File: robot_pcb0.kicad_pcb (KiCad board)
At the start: 2 copper layers, 74 parts, among them J1 USB_B_Mini, J10 GPIO, J2 CAN, J3 PWR, J4 Power_terminal, J5 Motor1, J6 Motor2, J7 Motor3, J8 Motor4, J9 UART, P1 SWD, U1 TJA1051TK-3, U2 STM32F40X_LQFP64, U3 MPU9250, U4 MCP16311/2, U5 MCP16311/2, U6 DRV8833PW, U7 DRV8833PW, Y1 8M

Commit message: some routing
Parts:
- moved C19 1.08 mm to (131.6, 95.2)
- moved C17 0.89 mm to (135.1, 95.2)
- turned C30 to 0 degrees
- turned C32 to 0 degrees
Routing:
- net Net-(C21-Pad2): track 0.00 -> 8.27 mm
- net Net-(R6-Pad1): track 0.00 -> 6.70 mm
- net Net-(C22-Pad2): track 0.00 -> 5.19 mm
- net 5V: track 0.00 -> 4.37 mm
- net Net-(C21-Pad1): track 0.00 -> 3.08 mm
- net Net-(C19-Pad1): track 0.00 -> 2.76 mm
- net V_IN: track 0.00 -> 0.77 mm
- net Net-(R7-Pad1): track 0.00 -> 0.57 mm
- added copper zone on B.Cu, net GND
- added copper zone on F.Cu, net VCC
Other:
- board outline added: 63.5 x 59.7 mm

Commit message: small amount of routing
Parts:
- moved C19 6.15 mm to (130.5, 89.2), turned to 90 degrees
- moved C17 4.56 mm to (136.2, 90.8), turned to 90 degrees
- moved R6 2.45 mm to (127.9, 88.5)
- moved R8 2.17 mm to (127.9, 91.3), turned to 180 degrees
- moved C29 1.49 mm to (99.6, 109.3)
- moved C31 1.32 mm to (96.5, 109.3), turned to 180 degrees
- moved C28 0.94 mm to (101.9, 111.8)
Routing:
- net VCC: track 0.05 -> 41.6 mm
- net GND: track 15.3 -> 43.0 mm
- net Net-(J8-Pad2): track 0.00 -> 18.8 mm
- net Net-(J8-Pad1): track 0.00 -> 12.6 mm
- net 5V: track 4.37 -> 13.7 mm
- net Net-(J7-Pad2): track 0.00 -> 9.28 mm
- net Net-(J7-Pad1): track 0.00 -> 7.75 mm
- net V_IN: track 0.77 -> 6.92 mm
- net Net-(C28-Pad2): track 0.00 -> 4.22 mm
- net Net-(R6-Pad1): track 6.70 -> 9.20 mm
- net Net-(C19-Pad1): track 2.76 -> 4.32 mm
- removed copper zone on B.Cu, net GND
- removed copper zone on F.Cu, net VCC

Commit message: update
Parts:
- removed C14: 100n, Capacitor_SMD:C_0603_1608Metric
- R11: value 51k -> 56k
- U3: value MPU9250 -> BMI160; footprint crf1:QFN-24-1EP_3x3mm_P0.4mm_nopp -> Package_LGA:Bosch_LGA-14_3x2.5mm_P0.5mm
- moved R10 37.3 mm to (99.3, 119.4), turned to 0 degrees
- moved R3 7.73 mm to (100.1, 78.7), turned to 180 degrees
- moved C19 6.15 mm to (131.6, 95.2), turned to 180 degrees
- moved C13 4.49 mm to (108.6, 107.7), turned to 0 degrees
- moved C6 4.39 mm to (111.1, 107.2), turned to 270 degrees
- moved U3 2.87 mm to (108.4, 105.2)
- moved C11 2.76 mm to (112.3, 99.1), turned to 180 degrees
- moved R8 2.69 mm to (129.8, 93.2), turned to 0 degrees
- moved R5 2.52 mm to (106.0, 101.3), turned to 180 degrees
- moved R6 2.45 mm to (128.2, 90.9)
- moved C16 2.00 mm to (112.2, 84.1), turned to 0 degrees
- moved R4 1.65 mm to (109.3, 101.3), turned to 0 degrees
- moved C29 1.49 mm to (100.3, 108.0)
- moved C31 1.32 mm to (96.5, 108.0), turned to 0 degrees
- moved C28 0.94 mm to (102.9, 111.8)
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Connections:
- U2 pad 57: Net-(U2-Pad57) -> IMU_INT2
- U3 pad 1: VCC -> GND
- U3 pad 11: GND -> Net-(U3-Pad11)
- U3 pad 12: Net-(U3-Pad12) -> VCC
- U3 pad 13: VCC -> SCL
- U3 pad 14: (no net) -> SDA
- U3 pad 2: (no net) -> Net-(U3-Pad2)
- U3 pad 3: (no net) -> Net-(U3-Pad3)
- U3 pad 4: (no net) -> Net-(U3-Pad4)
- U3 pad 5: (no net) -> VCC
- U3 pad 6: (no net) -> GND
- U3 pad 7: Net-(U3-Pad7) -> GND
- U3 pad 9: GND -> IMU_INT2
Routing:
- net VCC: track 41.6 -> 7.31 mm
- net CANL: track 0.00 -> 27.6 mm, vias 0 -> 2
- net CANH: track 0.00 -> 26.2 mm, vias 0 -> 2
- net GPIO0: track 0.00 -> 20.7 mm
- net GPIO1: track 0.00 -> 20.1 mm
- net GPIO6: track 0.00 -> 18.9 mm, vias 0 -> 1
- net Net-(J8-Pad2): track 18.8 -> 0.00 mm
- net GPIO7: track 0.00 -> 18.0 mm, vias 0 -> 1
- net GPIO2: track 0.00 -> 17.3 mm
- net GPIO4: track 0.00 -> 16.6 mm
- net GPIO3: track 0.00 -> 16.6 mm
- net GPIO5: track 0.00 -> 16.0 mm
- net 5V: track 13.7 -> 0.00 mm
- net Net-(J8-Pad1): track 12.6 -> 0.00 mm
- net GND: track 43.0 -> 30.5 mm, vias 2 -> 0
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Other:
- board outline removed

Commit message: routing
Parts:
- moved C30 21.7 mm to (99.7, 108.6), turned to 90 degrees
- moved C29 21.0 mm to (121.3, 108.4), turned to 90 degrees
- moved R10 15.7 mm to (101.9, 103.9)
- moved C15 10.0 mm to (94.3, 91.5), turned to 180 degrees
- moved C9 8.40 mm to (117.3, 88.1)
- moved U1 5.69 mm to (94.2, 94.7), turned to 90 degrees
- moved C18 5.55 mm to (135.6, 111.8), turned to 90 degrees
- moved C20 5.11 mm to (130.3, 112.0), turned to 90 degrees
- moved C19 4.44 mm to (130.6, 90.9), turned to 90 degrees
- moved R11 4.17 mm to (121.9, 103.6), turned to 270 degrees
- moved C2 3.85 mm to (94.3, 97.8), turned to 180 degrees
- moved C27 3.62 mm to (123.1, 108.4)
- moved C28 3.49 mm to (101.4, 108.6)
- moved R8 2.51 mm to (128.0, 91.4)
- moved R12 1.70 mm to (119.1, 103.6), turned to 270 degrees
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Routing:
- net GND: track 30.5 -> 297.3 mm, vias 0 -> 4
- net VCC: track 7.31 -> 169.7 mm, vias 0 -> 5
- net 5V: track 0.00 -> 111.4 mm, vias 0 -> 5
- net V_IN: track 0.00 -> 88.4 mm, vias 0 -> 3
- net DRV_nFAULT: track 0.00 -> 64.1 mm, vias 0 -> 4
- net DRV_BIN2_1: track 0.00 -> 35.4 mm, vias 0 -> 4
- net NRST: track 0.00 -> 34.2 mm, vias 0 -> 2
- net DRV_BIN1_1: track 0.00 -> 31.7 mm, vias 0 -> 4
- net DRV_AIN1_2: track 0.00 -> 28.7 mm, vias 0 -> 2
- net UART_RXD: track 0.00 -> 28.3 mm, vias 0 -> 1
- net UART_TXD: track 0.00 -> 28.2 mm, vias 0 -> 1
- net DRV_AIN2_1: track 0.00 -> 28.0 mm, vias 0 -> 2
- net DRV_AIN1_1: track 0.00 -> 27.8 mm, vias 0 -> 2
- net DRV_AIN2_2: track 0.00 -> 26.3 mm, vias 0 -> 2
- net DRV_BIN1_2: track 0.00 -> 25.7 mm, vias 0 -> 2
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
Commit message: routed and filled
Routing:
- net VCC: track 169.7 -> 277.3 mm, vias 5 -> 11
- net GND: track 297.3 -> 373.7 mm, vias 4 -> 21
- net 5V: track 111.4 -> 129.6 mm, vias 5 -> 3
- net IMU_INT2: track 16.4 -> 15.3 mm
- net SWCLK: track 17.1 -> 18.0 mm
- net UART_TXD: track 28.2 -> 29.0 mm
- net UART_RXD: track 28.3 -> 29.0 mm
- net SWDIO: track 21.3 -> 21.9 mm
- added copper zone on B.Cu, net GND
- added copper zone on F.Cu, net GND
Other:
- board outline added: 61.9 x 57.8 mm

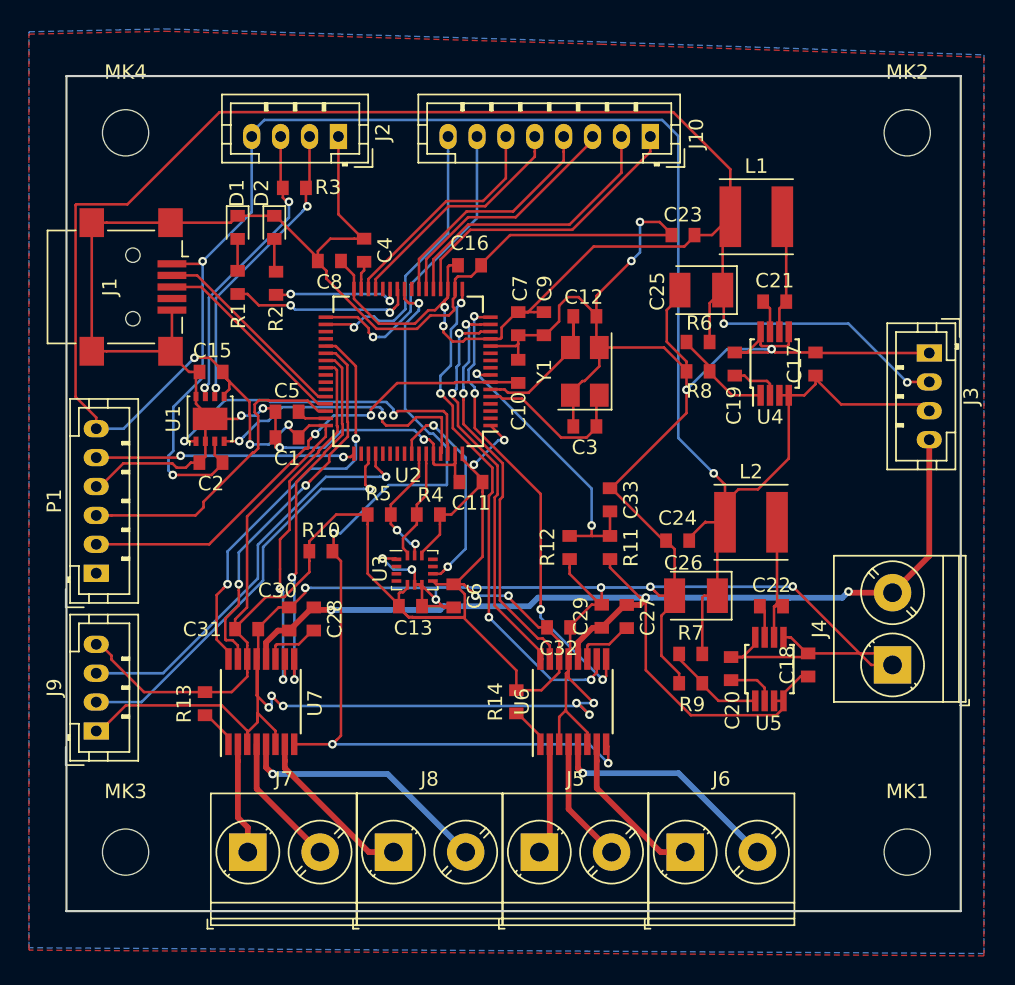
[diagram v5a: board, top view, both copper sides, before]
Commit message: added some extra vias and shortened a 5V path
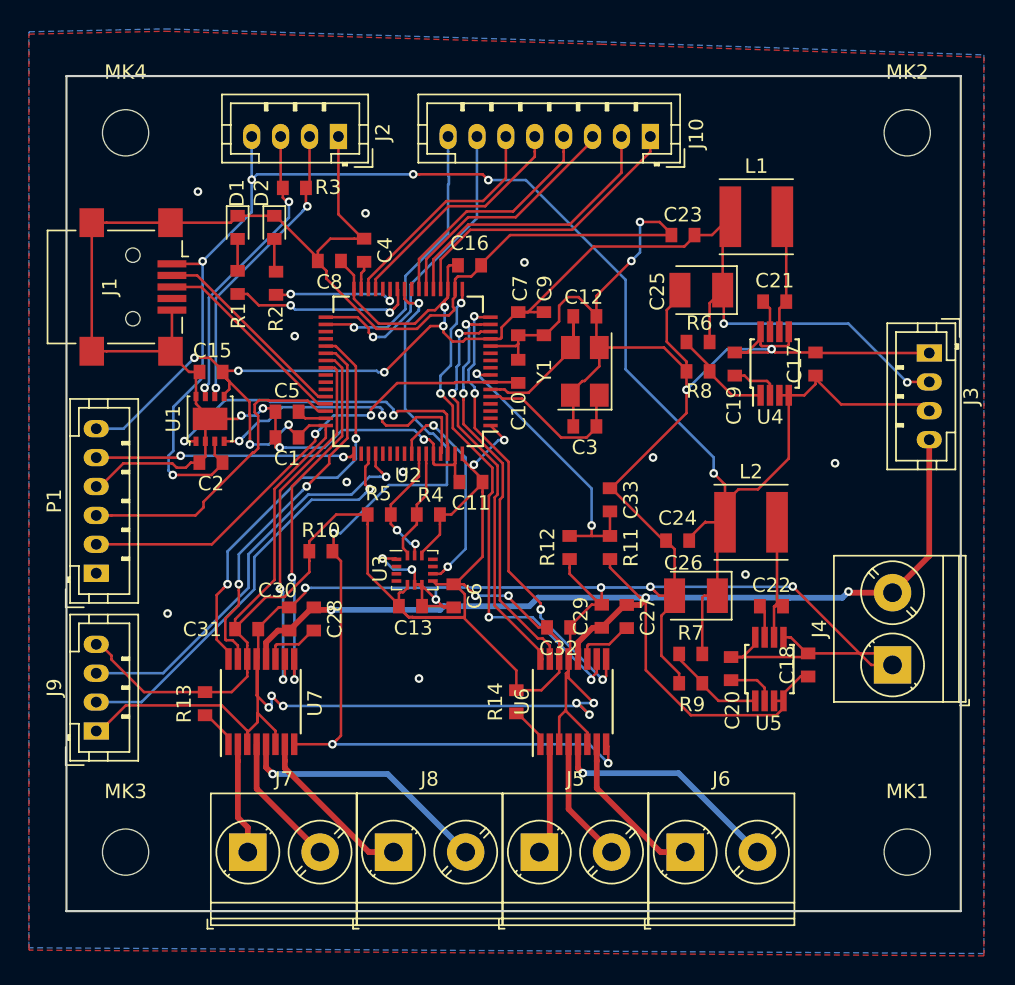
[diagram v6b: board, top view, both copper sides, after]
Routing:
- net VCC: track 277.3 -> 225.0 mm, vias 11 -> 13
- net 5V: track 129.6 -> 119.6 mm, vias 3 -> 6
- net GND: vias 21 -> 32

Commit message: rounded corners and some more vias between groundplanes
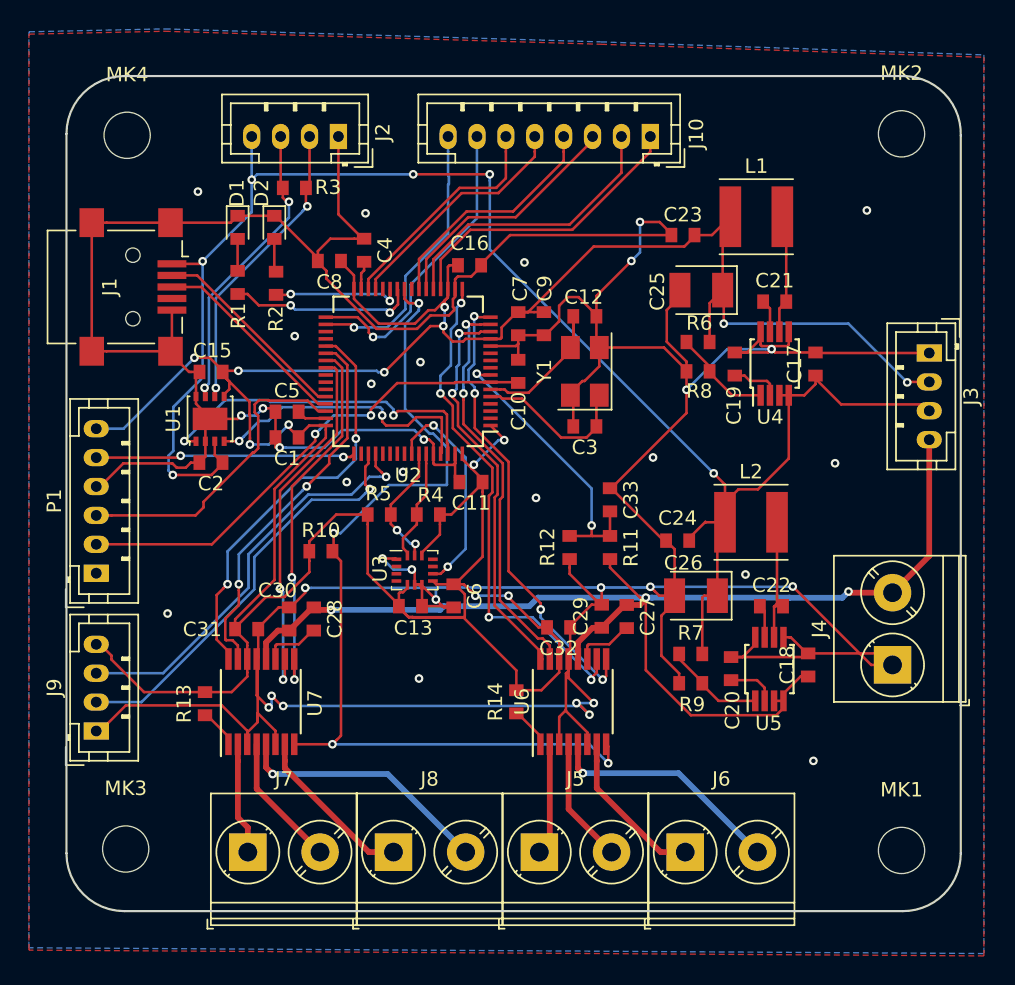
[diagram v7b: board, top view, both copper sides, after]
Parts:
- moved MK1 0.41 mm to (142.1, 124.6)
- moved MK2 0.40 mm to (142.1, 75.0)
- moved MK3 0.21 mm to (88.4, 124.5)
- moved MK4 0.20 mm to (88.5, 75.1)
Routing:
- net 5V: track 119.6 -> 118.4 mm
- net GND: vias 32 -> 37
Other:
- outline, holes or cut-outs redrawn
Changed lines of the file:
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@@
   (general
     (thickness 1.6)
-    (drawings 4)
-    (tracks 1098)
+    (drawings 8)
+    (tracks 1100)
     (modules 73)
     (nets 90)
@@
   )
   (module "MountingHole:MountingHole_3.2mm_M3" (layer "F.Cu")
-    (at 142.494 124.714)
+    (at 142.1 124.6)
     (descr "Mounting Hole 3.2mm, no annular, M3")
     (tags "mounting hole 3.2mm no annular m3")
@@
   )
   (module "MountingHole:MountingHole_3.2mm_M3" (layer "F.Cu")
-    (at 142.494 74.93)
+    (at 142.1 75)
     (descr "Mounting Hole 3.2mm, no annular, M3")
     (tags "mounting hole 3.2mm no annular m3")
@@
   )
   (module "MountingHole:MountingHole_3.2mm_M3" (layer "F.Cu")
-    (at 88.392 124.714)
+    (at 88.4 124.5)
     (descr "Mounting Hole 3.2mm, no annular, M3")
     (tags "mounting hole 3.2mm no annular m3")
@@
   )
   (module "MountingHole:MountingHole_3.2mm_M3" (layer "F.Cu")
-    (at 88.392 74.93)
+    (at 88.5 75.1)
     (descr "Mounting Hole 3.2mm, no annular, M3")
     (tags "mounting hole 3.2mm no annular m3")
@@
     )
   )
-  (gr_line (start 84.3 71) (end 146.2 71) (layer "Edge.Cuts") (width 0.15))
-  (gr_line (start 84.3 128.8) (end 84.3 71) (layer "Edge.Cuts") (width 0.15))
-  (gr_line (start 146.2 128.8) (end 84.3 128.8) (layer "Edge.Cuts") (width 0.15))
-  (gr_line (start 146.2 71) (end 146.2 128.8) (layer "Edge.Cuts") (width 0.15))
+  (gr_line (start 146.2 124.8) (end 146.199999 75.099999) (layer "Edge.Cuts") (width 0.15))
+  (gr_line (start 88.3 128.8) (end 142.2 128.8) (layer "Edge.Cuts") (width 0.15))
+  (gr_line (start 84.3 75) (end 84.3 124.8) (layer "Edge.Cuts") (width 0.15))
+  (gr_line (start 142.199999 70.998751) (end 88.3 71) (layer "Edge.Cuts") (width 0.15))
+  (gr_arc (start 142.2 124.8) (end 142.2 128.8) (angle -90) (layer "Edge.Cuts") (width 0.15))
+  (gr_arc (start 88.3 124.8) (end 84.3 124.8) (angle -90) (layer "Edge.Cuts") (width 0.15))
+  (gr_arc (start 88.3 75) (end 88.3 71) (angle -90) (layer "Edge.Cuts") (width 0.15))
+  (gr_arc (start 142.2 75) (end 146.199999 75.099999) (angle -91.43209618) (layer "Edge.Cuts") (width 0.15))
   (segment (start 117.755 123.9895) (end 117.0305 124.714) (width 0.4) (layer "F.Cu") (net 1))
   (segment (start 117.755 117.25) (end 117.755 123.9895) (width 0.4) (layer "F.Cu") (net 1))
@@
   (via (at 137.5 97.8) (size 0.6) (drill 0.3) (layers "F.Cu" "B.Cu") (net 8))
   (via (at 131.3 105.5) (size 0.6) (drill 0.3) (layers "F.Cu" "B.Cu") (net 8))
+  (via (at 136 118.4) (size 0.6) (drill 0.3) (layers "F.Cu" "B.Cu") (net 8))
+  (via (at 139.7 80.3) (size 0.6) (drill 0.3) (layers "F.Cu" "B.Cu") (net 8))
+  (via (at 108.8 90.8) (size 0.6) (drill 0.3) (layers "F.Cu" "B.Cu") (net 8))
+  (via (at 105.4 92.3) (size 0.6) (drill 0.3) (layers "F.Cu" "B.Cu") (net 8))
+  (via (at 116.8 100.2) (size 0.6) (drill 0.3) (layers "F.Cu" "B.Cu") (net 8))
   (segment (start 121.005 118.4) (end 121.005 117.25) (width 0.4) (layer "F.Cu") (net 9))
   (segment (start 121.005 120.292) (end 121.005 118.4) (width 0.4) (layer "F.Cu") (net 9))
@@
   (segment (start 129.881396 99.281396) (end 129.1 98.5) (width 0.18) (layer "F.Cu") (net 22))
   (segment (start 129.881396 101.885756) (end 129.881396 99.281396) (width 0.18) (layer "F.Cu") (net 22))
-  (segment (start 129.1 98.5) (end 129.1 97.4) (width 0.18) (layer "B.Cu") (net 22))
-  (segment (start 129.1 97.4) (end 123 91.3) (width 0.18) (layer "B.Cu") (net 22))
-  (segment (start 123 91.3) (end 123 85.1) (width 0.18) (layer "B.Cu") (net 22))
-  (via (at 113.5 78.2) (size 0.6) (drill 0.3) (layers "F.Cu" "B.Cu") (net 22))
-  (segment (start 123 85.1) (end 116.1 78.2) (width 0.18) (layer "B.Cu") (net 22))
-  (segment (start 116.1 78.2) (end 113.5 78.2) (width 0.18) (layer "B.Cu") (net 22))
-  (segment (start 113.5 78.2) (end 113.1 77.8) (width 0.18) (layer "F.Cu") (net 22))
   (via (at 108.3 77.8) (size 0.6) (drill 0.3) (layers "F.Cu" "B.Cu") (net 22))
-  (segment (start 108.724264 77.8) (end 108.3 77.8) (width 0.18) (layer "F.Cu") (net 22))
-  (segment (start 113.1 77.8) (end 108.724264 77.8) (width 0.18) (layer "F.Cu") (net 22))
   (segment (start 97.124 80.422) (end 97.124 78.176) (width 0.18) (layer "B.Cu") (net 22))
   (segment (start 97.124 78.176) (end 97.124 75.184) (width 0.18) (layer "B.Cu") (net 22))
@@
   (segment (start 97.5 77.8) (end 97.124 78.176) (width 0.18) (layer "B.Cu") (net 22))
   (segment (start 108.3 77.8) (end 97.5 77.8) (width 0.18) (layer "B.Cu") (net 22))
+  (segment (start 113.6 83) (end 113.6 78.224264) (width 0.18) (layer "B.Cu") (net 22))
+  (segment (start 113.6 78.224264) (end 113.6 77.8) (width 0.18) (layer "B.Cu") (net 22))
+  (segment (start 129.1 98.5) (end 113.6 83) (width 0.18) (layer "B.Cu") (net 22))
+  (via (at 113.6 77.8) (size 0.6) (drill 0.3) (layers "F.Cu" "B.Cu") (net 22))
+  (segment (start 108.3 77.8) (end 113.6 77.8) (width 0.18) (layer "F.Cu") (net 22))
   (via (at 102.79 102.64) (size 0.6) (drill 0.3) (layers "F.Cu" "B.Cu") (net 23))
   (segment (start 102.79 103.81) (end 102.71 103.89) (width 0.18) (layer "F.Cu") (net 23))
@@
   (segment (start 116.714 76.239) (end 116.714 75.184) (width 0.18) (layer "F.Cu") (net 58))
   (segment (start 116.714 76.581132) (end 116.714 76.239) (width 0.18) (layer "F.Cu") (net 58))
-  (segment (start 113.285132 80.01) (end 116.714 76.581132) (width 0.18) (layer "F.Cu") (net 58))
-  (segment (start 110.75 80.01) (end 113.285132 80.01) (width 0.18) (layer "F.Cu") (net 58))
-  (segment (start 105.7 85.06) (end 110.75 80.01) (width 0.18) (layer "F.Cu") (net 58))
   (segment (start 105.7 85.74) (end 105.7 85.06) (width 0.18) (layer "F.Cu") (net 58))
+  (segment (start 114.195132 79.1) (end 116.714 76.581132) (width 0.18) (layer "F.Cu") (net 58))
+  (segment (start 111.66 79.1) (end 114.195132 79.1) (width 0.18) (layer "F.Cu") (net 58))
+  (segment (start 105.7 85.06) (end 111.66 79.1) (width 0.18) (layer "F.Cu") (net 58))
+  (segment (start 111.510879 78.739989) (end 114.046011 78.739989) (width 0.18) (layer "F.Cu") (net 59))
   (segment (start 105.2 85.74) (end 105.2 85.050869) (width 0.18) (layer "F.Cu") (net 59))
-  (segment (start 110.600879 79.64999) (end 113.13601 79.64999) (width 0.18) (layer "F.Cu") (net 59))
-  (segment (start 105.2 85.050869) (end 110.600879 79.64999) (width 0.18) (layer "F.Cu") (net 59))
-  (segment (start 113.13601 79.64999) (end 114.714 78.072) (width 0.18) (layer "F.Cu") (net 59))
-  (segment (start 114.714 78.072) (end 114.714 75.184) (width 0.18) (layer "F.Cu") (net 59))
+  (segment (start 114.714 76.239) (end 114.714 75.184) (width 0.18) (layer "F.Cu") (net 59))
+  (segment (start 114.714 78.072) (end 114.714 76.239) (width 0.18) (layer "F.Cu") (net 59))
+  (segment (start 105.2 85.050869) (end 111.510879 78.739989) (width 0.18) (layer "F.Cu") (net 59))
+  (segment (start 114.046011 78.739989) (end 114.714 78.072) (width 0.18) (layer "F.Cu") (net 59))
   (segment (start 104.7 85.06) (end 104.7 85.74) (width 0.18) (layer "F.Cu") (net 60))
   (segment (start 104.7 84.65) (end 104.7 85.06) (width 0.18) (layer "F.Cu") (net 60))

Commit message: small tweaks
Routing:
- net V_IN: track 88.8 -> 102.3 mm, vias 3 -> 2
- net DRV_nFAULT: track 64.1 -> 67.7 mm
- net GND: track 373.7 -> 375.0 mm, vias 37 -> 38
